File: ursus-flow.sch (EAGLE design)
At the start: 22 parts

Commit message: Save circuit 2016/12/24
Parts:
- added 12V_PWR1: 22-23-2021, con-molex:22-23-2021
- added 1N4007: SM4007, _mod_diode:SM4007
- added C10, C11, C12, C13, C8, C9: 0.1uf, rcl:C-EUC0805
- added C14, C15: 2.2uf, rcl:C-EUC0805
- added C16, C17: 1uf, rcl:C-EUC0805
- added C7: 680uf, rcl:CPOL-USD/7343-31W
- added MT9V034: (no value), con-lstb:MA12-2
- added R10: 10k, resistor:R-EU_R0805W
- added R5, R6, R7, R8: 1k, rcl:R-EU_M0805
- added R9: (no value), resistor:R-EU_R0805W
- added SV1: (no value), con-lstb:MA04-1
- added SV3: (no value), con-lstb:MA06-1
- added U$3: MICRO-USB-RECEPTACLE47589-0001, usb_mirco_b:MICRO-USB-RECEPTACLE47589-0001
- added X1, X2, X4: 22-23-2041, con-molex:22-23-2041
- added X3: (no value), con-molex:22-23-2061
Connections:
- net DCMI_D1 renamed DCMI_SYSCLK
- new net AT24C08C_A2: U$1.PA9, U$2.A2
- new net LED_B: LED3.A, U$1.PD12
- new net LED_G: LED2.A, U$1.PD13
- new net LED_R: LED1.A, U$1.PD14
- new net MPU9250_SPI1_CS: SV3.4, U$1.PC4
- new net N$10: R7.1, X2-4.S
- new net N$11: R8.1, X2-3.S
- new net N$12: 1N4007.C, C5.1, IC1.IN
- new net N$13: C14.1, U$1.VCAP_1
- new net N$14: C15.2, U$1.VCAP_2
- new net N$15: R10.1, U$1.BOOT0
- new net N$5: C10.1, C11.1, C12.1, C13.1, C8.1, C9.1
- new net N$8: R5.1, X1-4.S
- new net N$9: R6.1, X1-3.S
- new net NRST: R9.1, U$1.NRST
- new net SPI2_CS: U$1.PC3
- new net SPI2_MISO: U$1.PC2, X3-3.S
- new net SPI2_MOSI: U$1.PC1, X3-4.S
- new net SPI2_SCK: U$1.PB13, X3-2.S
- new net STLINLK_SWCLK: SV1.2, U$1.PA14/SWCLK
- new net STLINLK_SWDIO: SV1.3, U$1.PA13/SWDIO
- new net UART2_RX: U$1.PA3
- new net UART2_TX: U$1.PA2
- new net UART3_RX: U$1.PD9
- new net UART3_TX: R5.2, U$1.PD8
- new net V_USB: U$3.1
- net +3V3: now also C10.2, C11.2, C12.2, C13.2, C16.1, C17.1, C8.2, C9.2, SV3.6, U$1.VREF+, X1-2.S, X3-5.S
- net +5V: now also C7.+, X2-2.S, X4-4.S
- net AT24C08C_I2C3_SCL: now also U$2.SCL
- net AT24C08C_I2C3_SDA: now also U$2.SDA
- net EXTERNAL_8V: now also 12V_PWR1-2.S
- net GND: now also 12V_PWR1-1.S, C14.2, C15.1, C16.2, C17.2, C7.-, R10.2, R9.2, SV1.1, SV3.5, U$3.5, U$3.GND1, U$3.GND2, U$3.GND3, U$3.GND4, X1-1.S, X2-1.S, X3-6.S, X4-1.S
- net INTERNAL_8V: now also SJ2.3
- net LIDAR_I2C2_SCL: now also X4-3.S
- net LIDAR_I2C2_SDA: now also X4-2.S
- net MPU9250_SPI1_MISO: now also SV3.1
- net MPU9250_SPI1_MOSI: now also SV3.2
- net MPU9250_SPI1_SCK: now also SV3.3
- net N$6: now also 1N4007.A; no longer C5.1, IC1.IN
- net USB_OTG_FS_DM: now also U$3.2
- net USB_OTG_FS_DP: now also U$3.3
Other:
- note added: "C_N"
- note added: "C_P"
- note added: "D0"
- note added: "D1"
- note added: "D2"
- note added: "D3"
- note added: "D4"
- note added: "D5"
- note added: "D6"
- note added: "D7"
- note added: "D8"
- note added: "D_9"
- note added: "D_N"
- note added: "D_P"
- note added: "EXP"
- note added: "FRU"
- note added: "GND"
- note added: "LED"
- note added: "LIV"
- note added: "Lidar"
- note added: "PCK"
- note added: "SCK"
- note added: "SDA"
- note added: "SPI2"
- note added: "UART2"
- note added: "UART3"
- note added: "VCC"
- note added: "Vcc is not connected for ST-Link"
- moved on the sheet: 12V_PWR-1, 12V_PWR-2, 3V3_REG1117, 5V_REG1117, C1, C2, C3, C4, C5, C6, IC1, LED1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

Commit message: Save 2016/12/24
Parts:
- removed 12V_PWR, 12V_PWR1: 22-23-2021, con-molex:22-23-2021
- removed 5V_REG1117: REG1117, burr-brown:REG1117
- removed IC1: (no value), 7808:7808
- removed MT9V034: (no value), con-lstb:MA12-2
- removed SJ2: (no value), sparkfun:SOLDERJUMPER_2WAYS
- removed USE_12V: SOLDERJUMPERNO, sparkfun:SOLDERJUMPERNO
- added 1N1: SM4007, _mod_diode:SM4007
- added 5V_PWR: 22-23-2021, con-molex:22-23-2021
- added C18: 0.1uf, rcl:C-EUC0805
- added R11, R12, R13, R14, R15, R16: 4.7k, resistor:R-EU_R0805W
- added R17: 10k, resistor:R-EU_R0805W
- added R18: 1k, resistor:R-EU_R0805W
- added S1: EVQPSL/Q, switch-panasonic:EVQPSL/Q
- added U$4: MT9V034_MODULE, MT9V034_MODULE:MT9V034_MODULE
- added U$5: 8MHZ_CRYSTAL, 8MHZ_CRYSTAL:8MHZ_CRYSTAL
- C17: value 1uf -> 0.1uf
- C3, C4: value 10uf -> 20pf; device rcl:C-EUC0805K -> rcl:C-EUC0805
- C5, C6: value 10uf -> 0.1uf; device rcl:C-EUC0805K -> rcl:C-EUC0805
- R1, R2, R3, R4: value (none) -> 220
- R9: value (none) -> 10k
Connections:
- removed net 8V: 5V_REG1117.VIN, C4.1, SJ2.2
- removed net EXTERNAL_8V: 12V_PWR1-2.S, SJ2.1
- removed net INTERNAL_8V: SJ2.3, USE_12V.2
- new net DCMI_D1: U$1.PA10, U$4.D1
- new net MT9V034_I2C1_SCL: R15.2, U$1.PB6, U$4.I2C_SCK
- new net MT9V034_I2C1_SDA: R13.2, U$1.PB9, U$4.I2C_SDA
- new net N$16: C17.1, S1.P, S1.P1
- new net N$17: R9.1, U$4.BYPASS_CLKIN_N
- new net N$18: R17.1, U$4.SER_DATAIN_N
- new net N$19: R18.2, U$1.PA9
- net +3V3: now also C18.1, C6.1, R11.1, R12.1, R13.1, R14.1, R15.1, R16.1, R17.2, R9.2, X2-2.S; no longer C17.1
- net +5V: now also 1N1.C, 1N4007.C, C5.2, U$4.VCC; no longer 5V_REG1117.VOUT, C3.1, X2-2.S
- net AT24C08C_A2: no longer U$1.PA9
- net AT24C08C_I2C3_SCL: now also R11.2
- net AT24C08C_I2C3_SDA: now also R16.2
- net DCMI_D0: now also U$4.D0
- net DCMI_D2: now also U$4.D2
- net DCMI_D3: now also U$4.D3
- net DCMI_D4: now also U$4.D4
- net DCMI_D5: now also U$4.D5
- net DCMI_D6: now also U$4.D6
- net DCMI_D7: now also U$4.D7
- net DCMI_D8: now also U$4.D8
- net DCMI_D9: now also U$4.D9
- net DCMI_HSYNC: now also U$4.LINE_VALID
- net DCMI_SYSCLK: now also U$4.SYSCLK
- net DCMI_VSYNC: now also U$4.FRAME_VALID
- net GND: now also 5V_PWR-1.S, C18.2, C5.1, S1.S, S1.S1, U$4.BYPASS_CLKIN_P, U$4.EXPOSURE, U$4.GND, U$4.SER_DATAIN_P, U$5.2, U$5.4; no longer 12V_PWR-1.S, 12V_PWR1-1.S, 5V_REG1117.GND, C5.2, IC1.GND, R9.2
- net LIDAR_I2C2_SCL: now also R12.2
- net LIDAR_I2C2_SDA: now also R14.2
- net N$12: now also C4.1, U$1.PH1/OSC_OUT, U$5.1; no longer 1N4007.C, C5.1, IC1.IN
- net N$6: now also 5V_PWR-2.S; no longer 12V_PWR-2.S
- net N$7: now also C3.1, U$1.PH0/OSC_IN, U$5.3; no longer C6.1, IC1.OUT, USE_12V.1
- net NRST: no longer R9.1
- net V_USB: now also 1N1.A
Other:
- note added: "MPU9250(Breakboard Module)"
- note added: "MT9V034(Module)"
- note added: "Power from UBEC (5V)"
- note added: "Ursus-flow optical flow sensor NCKU: 071 Lab PU: Shengwen Cheng email: shengwen1997.tw@gmail.com"
- note removed: "8V source selector Internal: Linear regulator External: Switching mode regulator"
- note removed: "C_N"
- note removed: "C_P"
- note removed: "D0"
- note removed: "D1"
- note removed: "D2"
- note removed: "D3"
- note removed: "D4"
- note removed: "D5"
- note removed: "D6"
- note removed: "D7"
- note removed: "D8"
- note removed: "D_9"
- note removed: "D_N"
- note removed: "D_P"
- note removed: "Disolder the pad when externel 8V power is using"
- note removed: "EXP"
- note removed: "FRU"
- note removed: "GND"
- note removed: "LED"
- note removed: "LIV"
- note removed: "PCK"
- note removed: "SCK"
- note removed: "SDA"
- note removed: "Ursus-flow optical flow sensor NCKU: 071 Lab PU: Shengwen Cheng email: shengwen1997.tw@gmail.com [Note] MT9V034(Camera): I2C1, DCMI LIDAR: I2C2 AT24C08C(EEPROM): I2C3 MPU9250(IMU): SPI1, GPIO Full speed USB (Device mode only) UART2: Flight control board communication UART3 and SPI2 for alternated functions"
- note removed: "VCC"
- moved on the sheet: 1N4007, 3V3_REG1117, C1, C10, C11, C12, C13, C14, C15, C16, C17, C2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

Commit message: Save 2016/12/25 Happy Christmas
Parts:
- added C19, C20: 100uf/10V, rcl:CPOL-USB/3528-21W
- C7: value 680uf -> 680uf/10V
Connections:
- net +3V3: now also C20.+
- net +5V: now also C19.+
- net GND: now also C19.-, C20.-
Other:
- moved on the sheet: 1N1, 3V3_REG1117, C1, C2, U$3

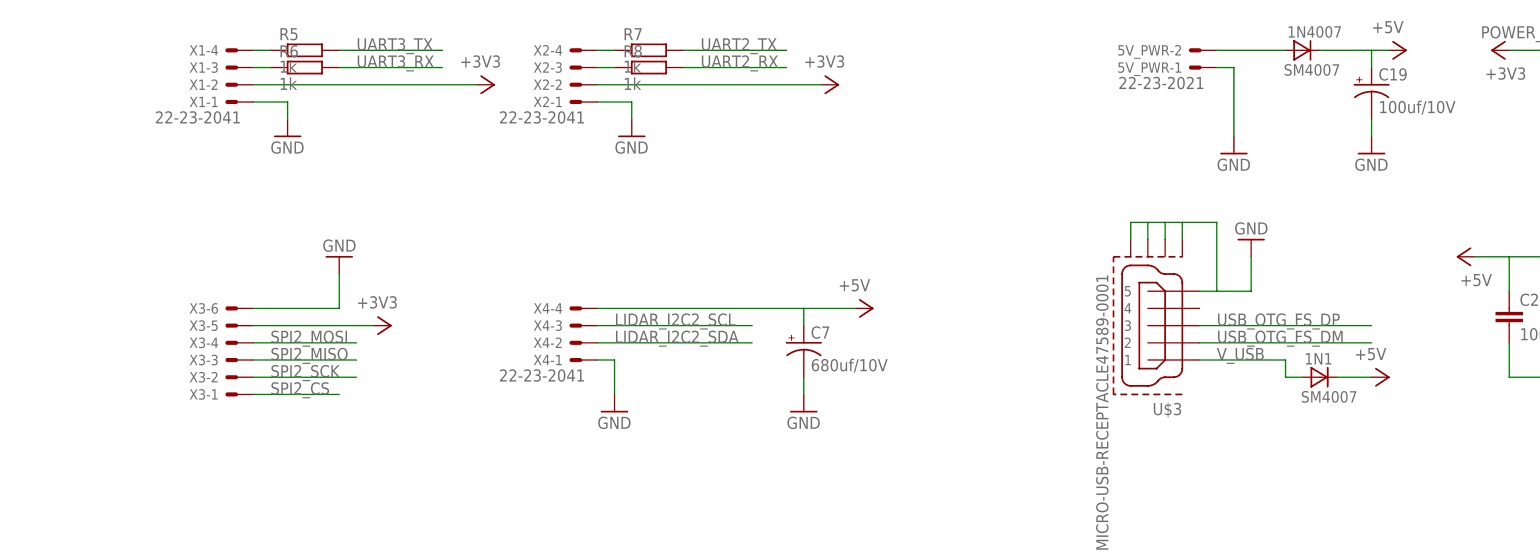
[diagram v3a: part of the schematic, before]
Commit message: Fix diode and connector
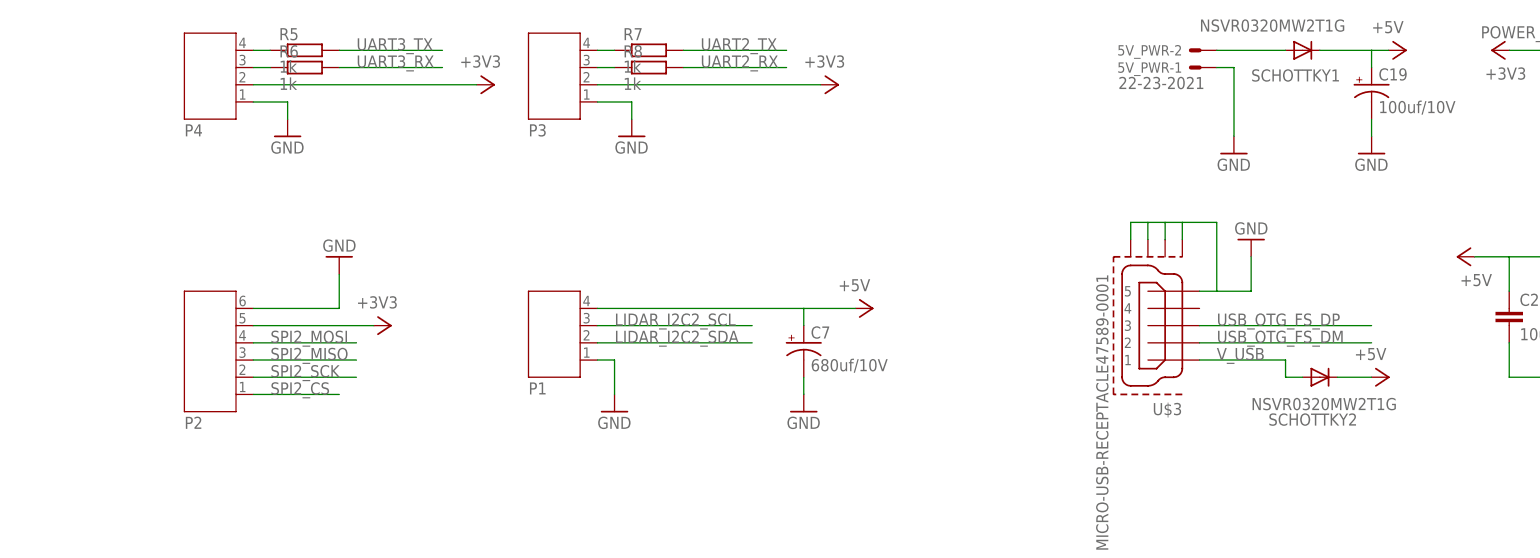
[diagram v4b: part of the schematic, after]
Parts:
- removed 1N1, 1N4007: SM4007, _mod_diode:SM4007
- removed X1, X2, X4: 22-23-2041, con-molex:22-23-2041
- removed X3: (no value), con-molex:22-23-2061
- added P1, P3, P4: (no value), jst-ph:JST-PH4
- added P2: (no value), jst-ph:JST-PH6
- added SCHOTTKY1, SCHOTTKY2: NSVR0320MW2T1G, _mod_diode:DIODE-SOD323-W
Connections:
- net +3V3: now also P2.5, P3.2, P4.2; no longer X1-2.S, X2-2.S, X3-5.S
- net +5V: now also P1.4, SCHOTTKY1.C, SCHOTTKY2.C; no longer 1N1.C, 1N4007.C, X4-4.S
- net GND: now also P1.1, P2.6, P3.1, P4.1; no longer X1-1.S, X2-1.S, X3-6.S, X4-1.S
- net LIDAR_I2C2_SCL: now also P1.3; no longer X4-3.S
- net LIDAR_I2C2_SDA: now also P1.2; no longer X4-2.S
- net N$10: now also P3.4; no longer X2-4.S
- net N$11: now also P3.3; no longer X2-3.S
- net N$6: now also SCHOTTKY1.A; no longer 1N4007.A
- net N$8: now also P4.4; no longer X1-4.S
- net N$9: now also P4.3; no longer X1-3.S
- net SPI2_CS: now also P2.1
- net SPI2_MISO: now also P2.3; no longer X3-3.S
- net SPI2_MOSI: now also P2.4; no longer X3-4.S
- net SPI2_SCK: now also P2.2; no longer X3-2.S
- net V_USB: now also SCHOTTKY2.A; no longer 1N1.A

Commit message: 2016/12/30 Good bye 2016
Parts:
- added TEST_PAD1, TEST_PAD2: TPSQTP20SQ, testpad:TPSQTP20SQ
- added U$10, U$7, U$8, U$9: M3_HOLE, M3_HOLE:M3_HOLE
- added U$6: LIDAR_MOUNT, LIDAR_MOUNT:LIDAR_MOUNT
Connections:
- net AT24C08C_I2C3_SCL: now also TEST_PAD2.TP
- net AT24C08C_I2C3_SDA: now also TEST_PAD1.TP
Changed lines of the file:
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@@
 <part name="SCHOTTKY2" library="_mod_diode" deviceset="DIODE-" device="SOD323-W" value="NSVR0320MW2T1G"/>
 <part name="SCHOTTKY1" library="_mod_diode" deviceset="DIODE-" device="SOD323-W" value="NSVR0320MW2T1G"/>
+<part name="TEST_PAD1" library="testpad" deviceset="TPSQ" device="TP20SQ"/>
+<part name="TEST_PAD2" library="testpad" deviceset="TPSQ" device="TP20SQ"/>
+<part name="U$6" library="LIDAR_MOUNT" deviceset="LIDAR_MOUNT" device=""/>
+<part name="U$7" library="M3_HOLE" deviceset="M3_HOLE" device=""/>
+<part name="U$8" library="M3_HOLE" deviceset="M3_HOLE" device=""/>
+<part name="U$9" library="M3_HOLE" deviceset="M3_HOLE" device=""/>
+<part name="U$10" library="M3_HOLE" deviceset="M3_HOLE" device=""/>
 </parts>
 <sheets>
@@
 <attribute name="VALUE" x="22.86" y="211.0486" size="1.778" layer="96"/>
 </instance>
+<instance part="TEST_PAD1" gate="G$1" x="99.06" y="10.16" smashed="yes" rot="R90">
+<attribute name="NAME" x="111.76" y="14.605" size="1.778" layer="95" rot="R180"/>
+<attribute name="TP_SIGNAL_NAME" x="100.33" y="12.7" size="1.778" layer="97" rot="R90"/>
+</instance>
+<instance part="TEST_PAD2" gate="G$1" x="99.06" y="7.62" smashed="yes" rot="R90">
+<attribute name="NAME" x="109.22" y="4.445" size="1.778" layer="95" rot="R180"/>
+<attribute name="TP_SIGNAL_NAME" x="100.33" y="10.16" size="1.778" layer="97" rot="R90"/>
+</instance>
+<instance part="U$6" gate="G$1" x="25.4" y="-30.48"/>
+<instance part="U$7" gate="G$1" x="5.08" y="-58.42"/>
+<instance part="U$8" gate="G$1" x="17.78" y="-58.42"/>
+<instance part="U$9" gate="G$1" x="30.48" y="-58.42"/>
+<instance part="U$10" gate="G$1" x="43.18" y="-58.42"/>
 </instances>
 <busses>
@@
 </segment>
 <segment>
-<wire x1="93.98" y1="7.62" x2="66.04" y2="7.62" width="0.1524" layer="91"/>
+<wire x1="96.52" y1="7.62" x2="66.04" y2="7.62" width="0.1524" layer="91"/>
 <label x="68.58" y="7.62" size="1.778" layer="95"/>
 <pinref part="U$2" gate="G$1" pin="SCL"/>
+<pinref part="TEST_PAD2" gate="G$1" pin="TP"/>
 </segment>
 </net>
@@
 </segment>
 <segment>
-<wire x1="93.98" y1="10.16" x2="66.04" y2="10.16" width="0.1524" layer="91"/>
+<wire x1="96.52" y1="10.16" x2="66.04" y2="10.16" width="0.1524" layer="91"/>
 <label x="68.58" y="10.16" size="1.778" layer="95"/>
 <pinref part="U$2" gate="G$1" pin="SDA"/>
-</segment>
-</net>
+<pinref part="TEST_PAD1" gate="G$1" pin="TP"/>
+</segment>
+</net>

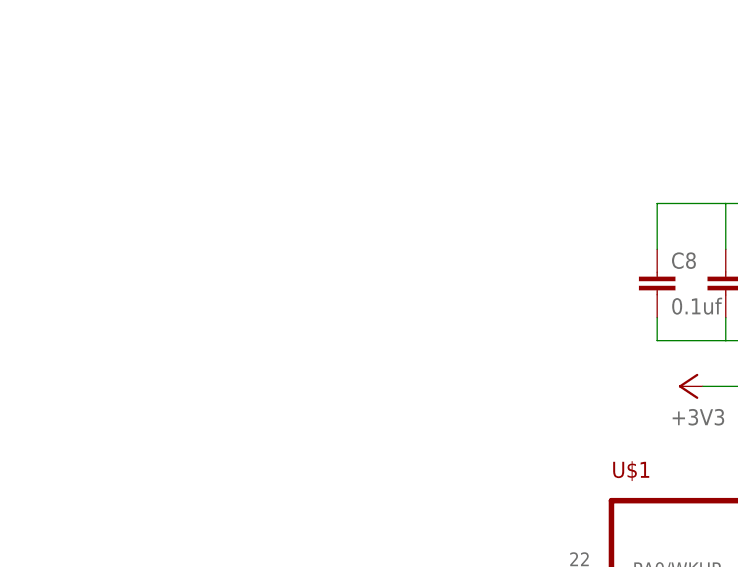
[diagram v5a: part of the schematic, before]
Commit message: Add MPU9250 breakout board
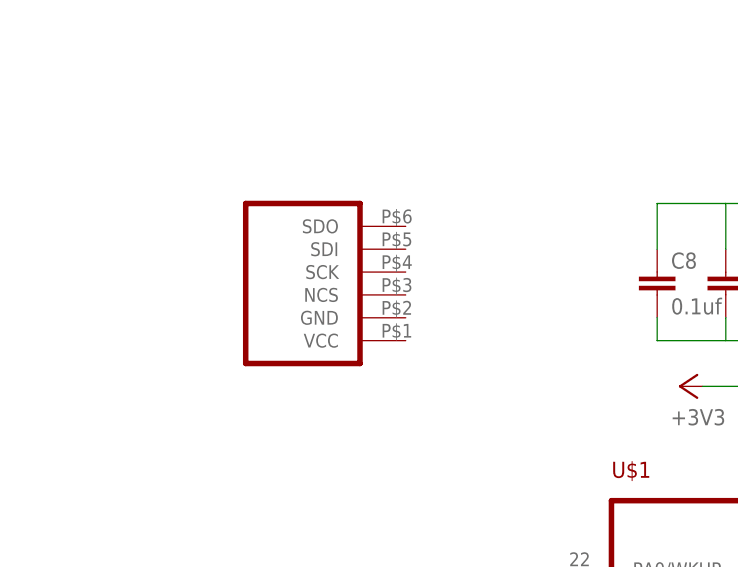
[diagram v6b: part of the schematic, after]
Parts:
- added U$11: MPU9250_BREAKOUT, MPU9250_BREAKOUT:MPU9250_BREAKOUT
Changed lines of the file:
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@@
 <part name="U$9" library="M3_HOLE" deviceset="M3_HOLE" device=""/>
 <part name="U$10" library="M3_HOLE" deviceset="M3_HOLE" device=""/>
+<part name="U$11" library="MPU9250_BREAKOUT" deviceset="MPU9250_BREAKOUT" device=""/>
 </parts>
 <sheets>
@@
 <instance part="U$9" gate="G$1" x="30.48" y="-58.42"/>
 <instance part="U$10" gate="G$1" x="43.18" y="-58.42"/>
+<instance part="U$11" gate="G$1" x="-132.08" y="116.84" rot="R180"/>
 </instances>
 <busses>
